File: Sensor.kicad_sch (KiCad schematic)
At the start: 21 parts, among them J10 I2C, J4 SHT, J5 I2C, J6 A_NO2, J7 UART1, J8 A_CO, J9 I2C, Q10 S8050, Q4 S8050, Q5 S8050, Q6 S8050, Q7 S8050, Q8 S8050, Q9 S8050

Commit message: [Fix] Schematic and layout. - Replaced STM32WLE5x symbol for better visualization of the symbols - Added some missing connections - Modified some components' values - Changed the layout for STM32WL
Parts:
- R21, R22, R23, R24, R25, R26, R27: footprint Resistor_SMD:R_0402_1005Metric_Pad0.72x0.64mm_HandSolder -> Resistor_SMD:R_0402_1005Metric

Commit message: Update PCB layout
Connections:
- net RX_PM: now also J7.3 (Pin_3); no longer J7.4 (Pin_4)
- net TX_PM: now also J7.4 (Pin_4); no longer J7.3 (Pin_3)
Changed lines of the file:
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@@
 	(hierarchical_label "RX_PM"
 		(shape input)
-		(at 137.16 53.34 0)
+		(at 137.16 55.88 0)
 		(fields_autoplaced yes)
 		(effects
@@
 	(hierarchical_label "TX_PM"
 		(shape input)
-		(at 137.16 55.88 0)
+		(at 137.16 53.34 0)
 		(fields_autoplaced yes)
 		(effects

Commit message: update problem
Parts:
- removed Q10, Q4: S8050, Package_TO_SOT_SMD:SOT-23, symbol Transistor_BJT:S8050
- added Q3, Q5: S8050, Package_TO_SOT_SMD:SOT-23, symbol Transistor_BJT:S8050
- J10, J5, J7, J9: footprint Connector_Molex:Molex_CLIK-Mate_502585-0470_1x04-1MP_P1.50mm_Horizontal -> Connector_Molex:Molex_CLIK-Mate_502443-0470_1x04-1MP_P2.00mm_Vertical
- renumbered Q5 to Q4, R21 to R20, R22 to R21, R23 to R22, R24 to R23, R25 to R24, R26 to R25, R27 to R26
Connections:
- net GND: now also Q4.2 (E), Q6.2 (E), Q7.2 (E), Q8.2 (E), Q9.2 (E), Q3.2 (E), Q5.2 (E); no longer Q4.1 (E), Q6.1 (E), Q7.1 (E), Q8.1 (E), Q9.1 (E)
- net at R20.2: now also Q3.1 (B)
- net at J5.2 (Pin_2): now also Q3.3 (C)
- net at R24.2: now also Q7.1 (B); no longer Q8.2 (B)
- net at J8.2 (Pin_2): now also Q7.3 (C); no longer Q8.3 (C)
- net at R22.2: now also Q5.1 (B); no longer Q6.2 (B)
- net at J10.2 (Pin_2): now also Q9.3 (C)
- net at R25.2: now also Q8.1 (B); no longer Q9.2 (B)
- net at J9.2 (Pin_2): now also Q8.3 (C); no longer Q9.3 (C)
- net at R23.2: now also Q6.1 (B); no longer Q7.2 (B)
- net at Q6.3 (C): now also J7.2 (Pin_2); no longer J6.2 (Pin_2)
- net at R21.1: now also Q4.1 (B); no longer Q4.2 (B)
- net at R26.2: now also Q9.1 (B)
- new net: J6.2 (Pin_2), Q5.3 (C)

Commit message: Update schematic
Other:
- moved on the sheet: J5, J6, J8, Q3, Q5, Q7, R20, R22, R24

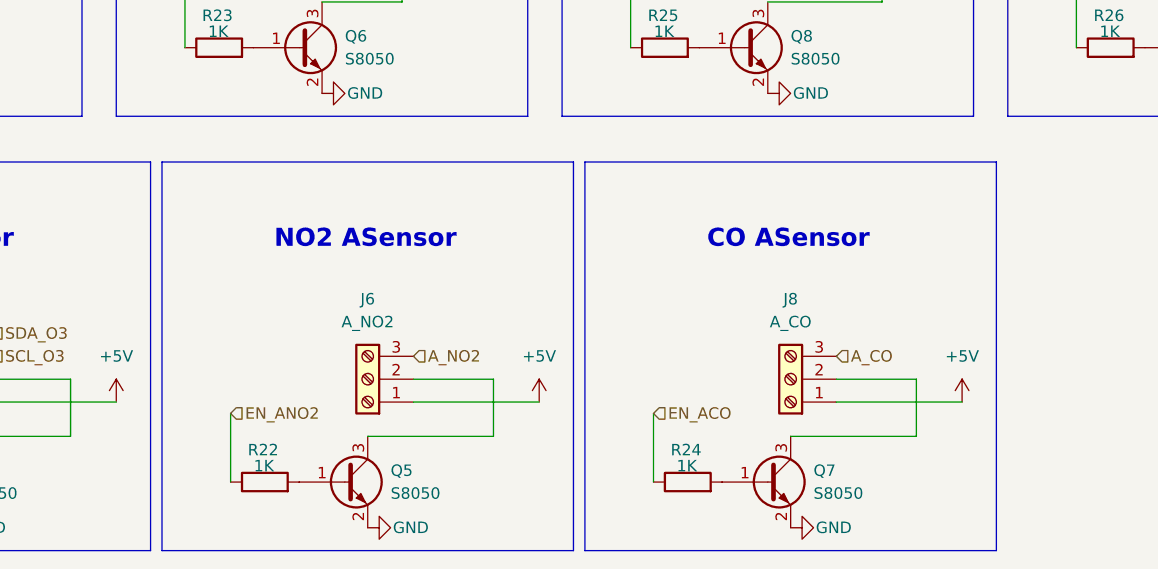
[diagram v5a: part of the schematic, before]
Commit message: Udpate test point
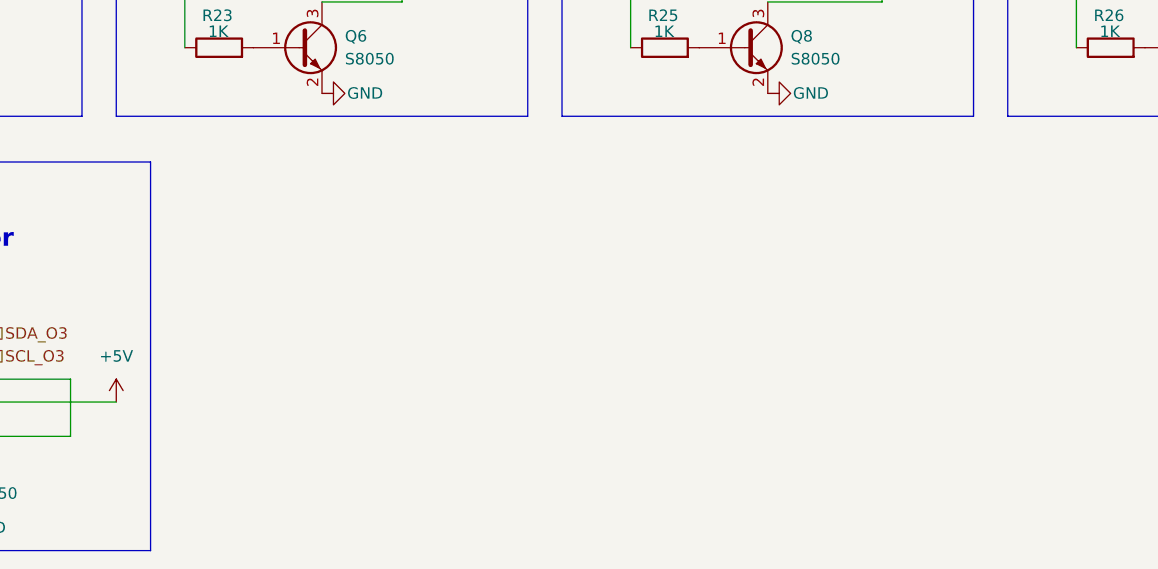
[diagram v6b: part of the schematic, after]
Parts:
- removed J6: A_NO2, Connector_JST:JST_XH_B3B-XH-A_1x03_P2.50mm_Vertical, symbol Connector:Screw_Terminal_01x03
- removed J8: A_CO, Connector_JST:JST_XH_B3B-XH-A_1x03_P2.50mm_Vertical, symbol Connector:Screw_Terminal_01x03
- removed Q5, Q7: S8050, Package_TO_SOT_SMD:SOT-23, symbol Transistor_BJT:S8050
- removed R22, R24: 1K, Resistor_SMD:R_0402_1005Metric, symbol Device:R
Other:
- note removed: "CO ASensor"
- note removed: "NO2 ASensor"

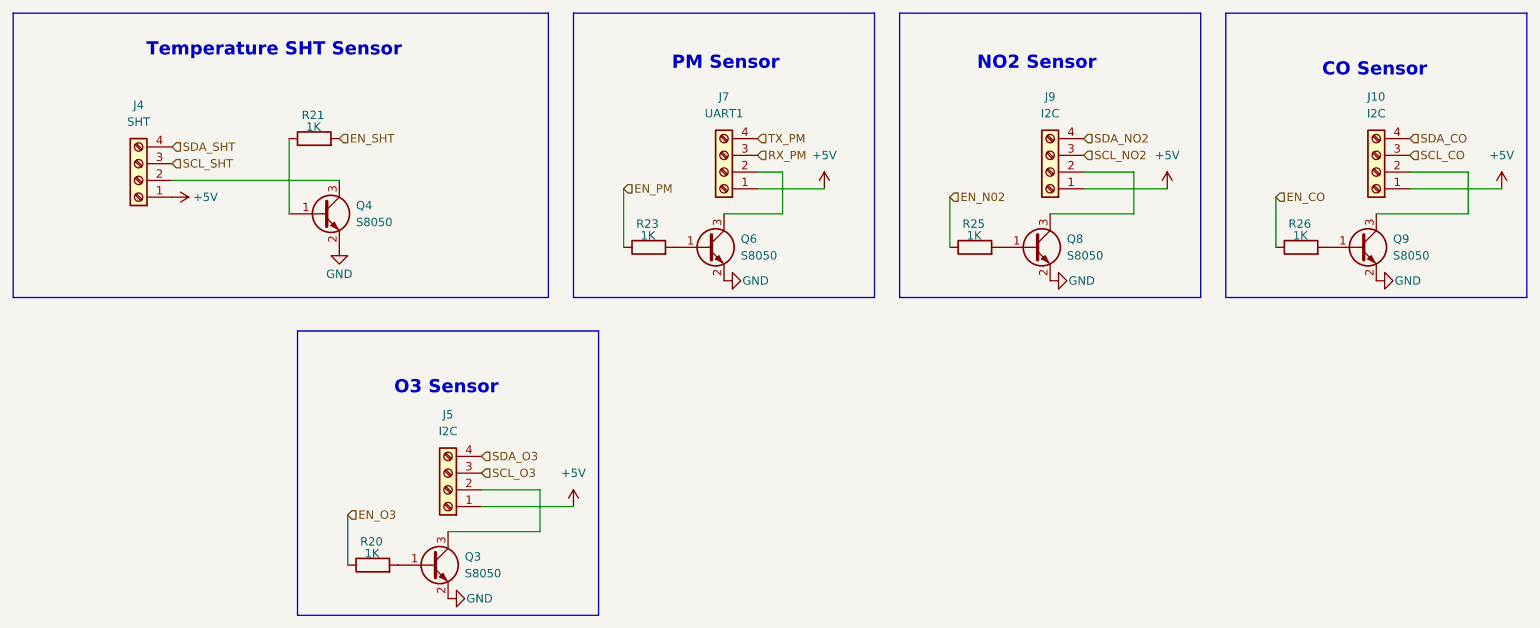
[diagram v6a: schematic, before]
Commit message: Update value resistor and transistor
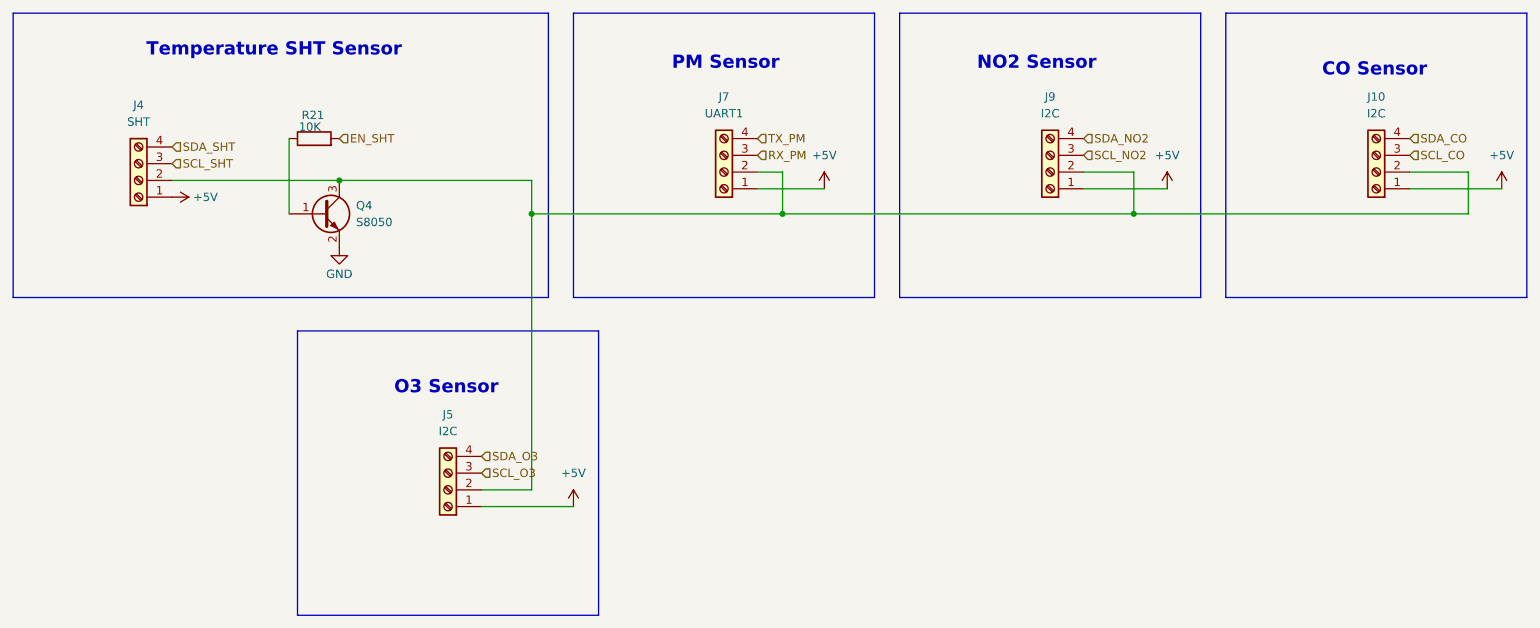
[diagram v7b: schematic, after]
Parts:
- removed Q3, Q6, Q8, Q9: S8050, Package_TO_SOT_SMD:SOT-23, symbol Transistor_BJT:S8050
- removed R20, R23, R25, R26: 1K, Resistor_SMD:R_0402_1005Metric, symbol Device:R
- R21: value 1K -> 10K
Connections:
- net at J10.2 (Pin_2): now also J4.2 (Pin_2), J5.2 (Pin_2), J7.2 (Pin_2), J9.2 (Pin_2), Q4.3 (C)
